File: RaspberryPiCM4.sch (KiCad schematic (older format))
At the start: 19 parts, among them U11 Compute_Module_4_Connectors

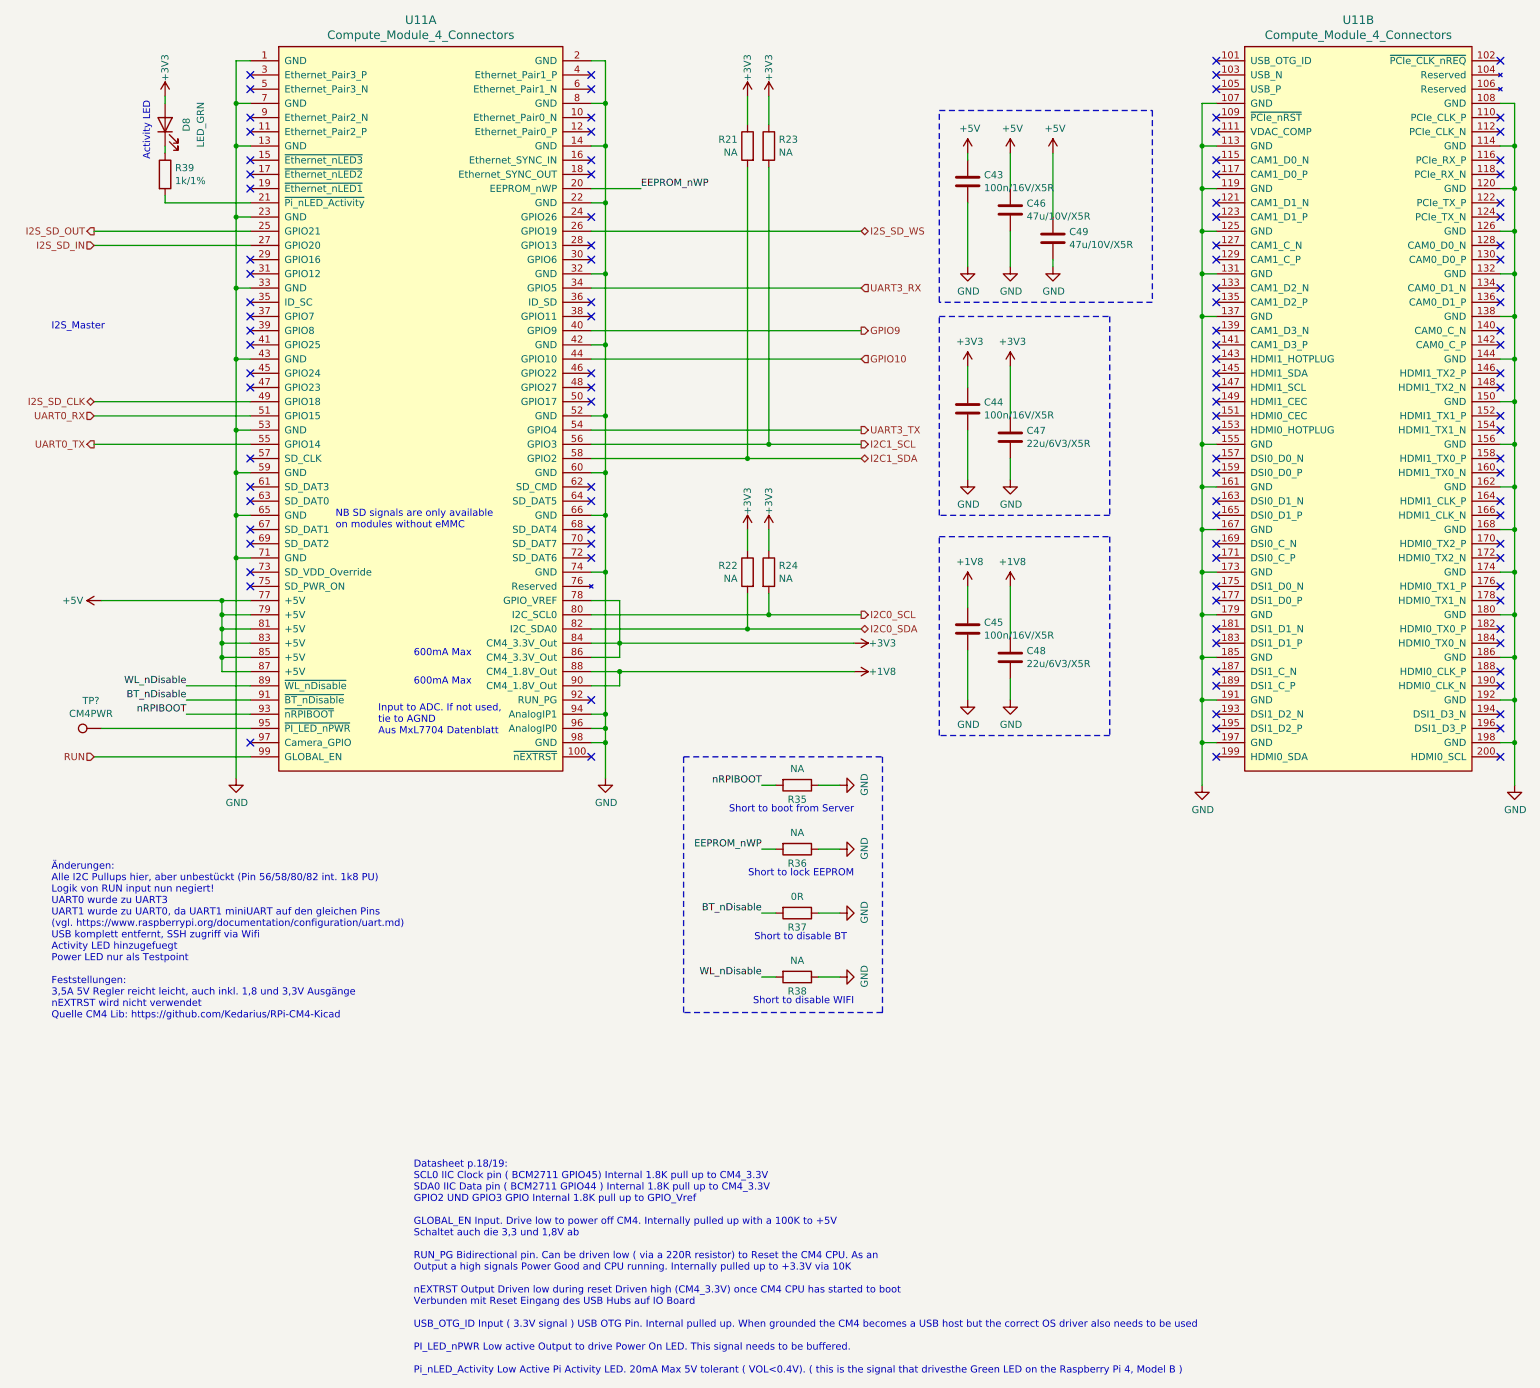
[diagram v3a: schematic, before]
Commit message: - ATmega überarbeitet - Alle offenen Punkte zusammengefasst
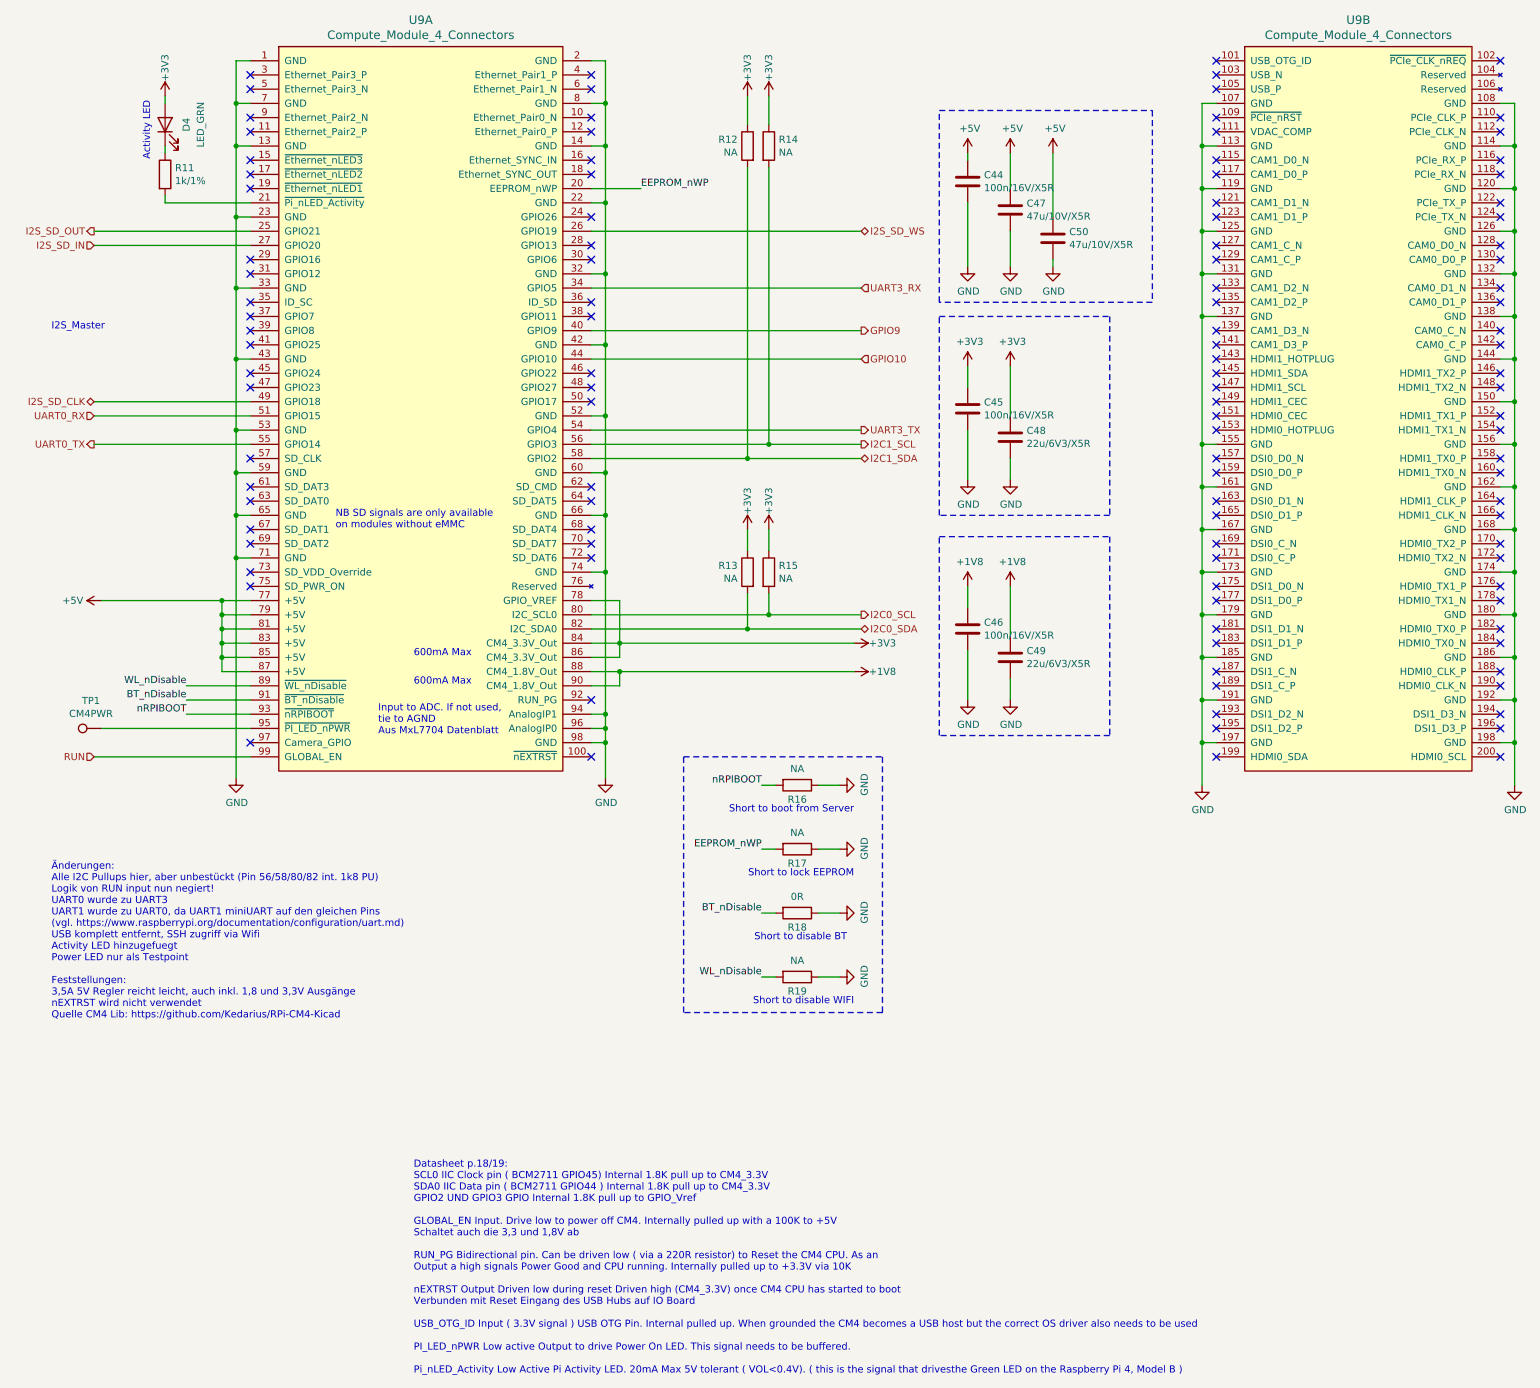
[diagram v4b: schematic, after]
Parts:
- gave numbers to parts that had none: 1
- renumbered C43 to C44, C44 to C45, C45 to C46, C46 to C47, C47 to C48, C48 to C49, C49 to C50, D8 to D4, R39 to R11, R21 to R12, R22 to R13, R23 to R14, R24 to R15, R35 to R16, R36 to R17, R37 to R18, R38 to R19, U11 to U9

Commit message: - Platzoptimierungen
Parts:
- C44, C45, C46: value 100n/16V/X5R -> 100n/16V/X7R; footprint Capacitor_SMD:C_0603_1608Metric -> Capacitor_SMD:C_0402_1005Metric
- C48, C49: footprint Capacitor_SMD:C_1206_3216Metric -> Capacitor_SMD:C_0805_2012Metric
- R16, R17, R18, R19: footprint Resistor_SMD:R_0402_1005Metric -> Resistor_SMD:R_0603_1608Metric
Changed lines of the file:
@@
 AR Path="/631EEDC8/60F304BE" Ref="C44"  Part="1"
 F 0 "C44" H 7265 1746 50  0000 L CNN
-F 1 "100n/16V/X5R" H 7265 1655 50  0000 L CNN
-F 2 "Capacitor_SMD:C_0603_1608Metric" H 7188 1550 50  0001 C CNN
+F 1 "100n/16V/X7R" H 7265 1655 50  0000 L CNN
+F 2 "Capacitor_SMD:C_0402_1005Metric" H 7188 1550 50  0001 C CNN
 F 3 "~" H 7150 1700 50  0001 C CNN
 	1    7150 1700
@@
 Wire Notes Line
 	6950 2550 6950 1200
-$Comp
-L Device:C C?
-U 1 1 61E27C6C
-P 7150 3300
-AR Path="/61E27C6C" Ref="C?"  Part="1"
-AR Path="/614D7E9D/61E27C6C" Ref="C?"  Part="1"
-AR Path="/631EEDC8/61E27C6C" Ref="C45"  Part="1"
-F 0 "C45" H 7265 3346 50  0000 L CNN
-F 1 "100n/16V/X5R" H 7265 3255 50  0000 L CNN
-F 2 "Capacitor_SMD:C_0603_1608Metric" H 7188 3150 50  0001 C CNN
-F 3 "~" H 7150 3300 50  0001 C CNN
-	1    7150 3300
-	1    0    0    -1
-$EndComp
-Wire Wire Line
-	7150 3450 7150 3800
 Wire Wire Line
 	7150 3000 7150 3150
@@
 F 0 "C48" H 7565 3546 50  0000 L CNN
 F 1 "22u/6V3/X5R" H 7565 3455 50  0000 L CNN
-F 2 "Capacitor_SMD:C_1206_3216Metric" H 7488 3350 50  0001 C CNN
+F 2 "Capacitor_SMD:C_0805_2012Metric" H 7488 3350 50  0001 C CNN
 F 3 "~" H 7450 3500 50  0001 C CNN
 	1    7450 3500
@@
 Wire Notes Line
 	6950 4050 6950 2650
-$Comp
-L Device:C C?
-U 1 1 61E3C7A7
-P 7150 4850
-AR Path="/61E3C7A7" Ref="C?"  Part="1"
-AR Path="/614D7E9D/61E3C7A7" Ref="C?"  Part="1"
-AR Path="/631EEDC8/61E3C7A7" Ref="C46"  Part="1"
-F 0 "C46" H 7265 4896 50  0000 L CNN
-F 1 "100n/16V/X5R" H 7265 4805 50  0000 L CNN
-F 2 "Capacitor_SMD:C_0603_1608Metric" H 7188 4700 50  0001 C CNN
-F 3 "~" H 7150 4850 50  0001 C CNN
-	1    7150 4850
-	1    0    0    -1
-$EndComp
 Wire Wire Line
 	7150 5000 7150 5350
@@
 F 0 "C49" H 7565 5096 50  0000 L CNN
 F 1 "22u/6V3/X5R" H 7565 5005 50  0000 L CNN
-F 2 "Capacitor_SMD:C_1206_3216Metric" H 7488 4900 50  0001 C CNN
+F 2 "Capacitor_SMD:C_0805_2012Metric" H 7488 4900 50  0001 C CNN
 F 3 "~" H 7450 5050 50  0001 C CNN
 	1    7450 5050
@@
 F 0 "R17" V 6050 6400 50  0000 C CNN
 F 1 "NA" V 5834 6400 50  0000 C CNN
-F 2 "Resistor_SMD:R_0402_1005Metric" V 5880 6400 50  0001 C CNN
+F 2 "Resistor_SMD:R_0603_1608Metric" V 5880 6400 50  0001 C CNN
 F 3 "~" H 5950 6400 50  0001 C CNN
 	1    5950 6400
@@
 F 0 "R18" V 6050 6850 50  0000 C CNN
 F 1 "0R" V 5834 6850 50  0000 C CNN
-F 2 "Resistor_SMD:R_0402_1005Metric" V 5880 6850 50  0001 C CNN
+F 2 "Resistor_SMD:R_0603_1608Metric" V 5880 6850 50  0001 C CNN
 F 3 "~" H 5950 6850 50  0001 C CNN
 	1    5950 6850
@@
 F 0 "R19" V 6050 7300 50  0000 C CNN
 F 1 "NA" V 5834 7300 50  0000 C CNN
-F 2 "Resistor_SMD:R_0402_1005Metric" V 5880 7300 50  0001 C CNN
+F 2 "Resistor_SMD:R_0603_1608Metric" V 5880 7300 50  0001 C CNN
 F 3 "~" H 5950 7300 50  0001 C CNN
 	1    5950 7300
@@
 F 0 "R16" V 6050 5950 50  0000 C CNN
 F 1 "NA" V 5834 5950 50  0000 C CNN
-F 2 "Resistor_SMD:R_0402_1005Metric" V 5880 5950 50  0001 C CNN
+F 2 "Resistor_SMD:R_0603_1608Metric" V 5880 5950 50  0001 C CNN
 F 3 "~" H 5950 5950 50  0001 C CNN
 	1    5950 5950
@@
 Wire Wire Line
 	1050 5550 2100 5550
+Wire Wire Line
+	7150 3450 7150 3800
+$Comp
+L Device:C C?
+U 1 1 60F997C5
+P 7150 3300
+AR Path="/60F997C5" Ref="C?"  Part="1"
+AR Path="/614D7E9D/60F997C5" Ref="C?"  Part="1"
+AR Path="/631EEDC8/60F997C5" Ref="C45"  Part="1"
+F 0 "C45" H 7265 3346 50  0000 L CNN
+F 1 "100n/16V/X7R" H 7265 3255 50  0000 L CNN
+F 2 "Capacitor_SMD:C_0402_1005Metric" H 7188 3150 50  0001 C CNN
+F 3 "~" H 7150 3300 50  0001 C CNN
+	1    7150 3300
+	1    0    0    -1
+$EndComp
+$Comp
+L Device:C C?
+U 1 1 60F9A018
+P 7150 4850
+AR Path="/60F9A018" Ref="C?"  Part="1"
+AR Path="/614D7E9D/60F9A018" Ref="C?"  Part="1"
+AR Path="/631EEDC8/60F9A018" Ref="C46"  Part="1"
+F 0 "C46" H 7265 4896 50  0000 L CNN
+F 1 "100n/16V/X7R" H 7265 4805 50  0000 L CNN
+F 2 "Capacitor_SMD:C_0402_1005Metric" H 7188 4700 50  0001 C CNN
+F 3 "~" H 7150 4850 50  0001 C CNN
+	1    7150 4850
+	1    0    0    -1
+$EndComp
 $EndSCHEMATC

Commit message: [mod:] BM83.MFB connection removed
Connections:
- net GPIO9: no longer names the net of U9.40 (GPIO9)
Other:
- note added: "Änderungen: \nAlle I2C Pullups hier, aber unbestückt (Pin 56/58/80/82 int. 1k8 PU)\nLogik von RUN input nun negiert!\nUART0 wurde zu UART3\nUART1 wurde zu UART0, da UART1 miniUART auf den gleichen Pins\n(vgl. https://www.raspberrypi.org/documentation/configuration/uart.md)\nUSB komplett entfernt, SSH zugriff via Wifi\nActivity LED hinzugefuegt\nPower LED nur als Testpoint\nGPIO9 entfernt, da BM83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"
- note removed: "Änderungen: \nAlle I2C Pullups hier, aber unbestückt (Pin 56/58/80/82 int. 1k8 PU)\nLogik von RUN input nun negiert!\nUART0 wurde zu UART3\nUART1 wurde zu UART0, da UART1 miniUART auf den gleichen Pins\n(vgl. https://www.raspberrypi.org/documentation/configuration/uart.md)\nUSB komplett entfernt, SSH zugriff via Wifi\nActivity LED hinzugefuegt\nPower LED nur als Testpoint\n\nFeststellungen: \n3,5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"
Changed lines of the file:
@@
 Wire Wire Line
 	1000 2050 2100 2050
-Text HLabel 6400 2750 2    50   Output ~ 0
-GPIO9
-Wire Wire Line
-	6400 2750 4500 2750
 Text HLabel 6400 2950 2    50   Input ~ 0
 GPIO10
@@
 $EndComp
 Text Notes 700  7600 0    50   ~ 0
-Änderungen: \nAlle I2C Pullups hier, aber unbestückt (Pin 56/58/80/82 int. 1k8 PU)\nLogik von RUN input nun negiert!\nUART0 wurde zu UART3\nUART1 wurde zu UART0, da UART1 miniUART auf den gleichen Pins\n(vgl. https://www.raspberrypi.org/documentation/configuration/uart.md)\nUSB komplett entfernt, SSH zugriff via Wifi\nActivity LED hinzugefuegt\nPower LED nur als Testpoint\n\nFeststellungen: \n3,5A 5V Regler reicht leicht, auch inkl. 1,8 und 3,3V Ausgänge\nnEXTRST wird nicht verwendet\nQuelle CM4 Lib: https://github.com/Kedarius/RPi-CM4-Kicad
+Änderungen: \nAlle I2C Pullups hier, aber unbestückt (Pin 56/58/80/82 int. 1k8 PU)\nLogik von RUN input nun negiert!\nUART0 wurde zu UART3\nUART1 wurde zu UART0, da UART1 miniUART auf den gleichen Pins\n(vgl. https://www.raspberrypi.org/documentation/configuration/uart.md)\nUSB komplett entfernt, SSH zugriff via Wifi\nActivity LED hinzugefuegt\nPower LED nur als Testpoint\nGPIO9 entfernt, da BM83.MFB nicht benötigt\n\nFeststellungen: \n3,5A 5V Regler reicht leicht, auch inkl. 1,8 und 3,3V Ausgänge\nnEXTRST wird nicht verwendet\nQuelle CM4 Lib: https://github.com/Kedarius/RPi-CM4-Kicad
 $Comp
 L Device:C C?
